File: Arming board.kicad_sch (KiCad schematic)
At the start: 22 parts, among them IC1 CD4043BDR, J3 Conn_01x04, Q1 SQS141ELNW-T1_GE3

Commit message: Basic routing and fixes
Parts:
- added H1, H2, H3, H4: MountingHole_Pad, MountingHole:MountingHole_3.2mm_M3_DIN965_Pad_TopBottom, symbol Mechanical:MountingHole_Pad
- C1, C2: value 1u -> 10u
- R3, R4: value 10k -> 1k
- R6, R7: value 10k -> 80k
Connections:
- net +BATT is gone; now on net VCC: D5.1 (K), D6.1 (K), J1.3 (Pin_3), J1.4 (Pin_4), J4.3 (Pin_3), J4.4 (Pin_4), Q1.1, Q1.2, Q1.3
- net GND: now also IC1.11 (R3), IC1.12 (S3), IC1.14 (S4), IC1.15 (R4), IC1.3 (R1), IC1.4 (S1), H1.1, H2.1, H3.1, H4.1
- net at D3.1 (K), R4.2: now also J3.3 (Pin_3); no longer J3.2 (Pin_2)
- net at D1.1 (K), R3.2: now also J3.2 (Pin_2); no longer J3.3 (Pin_3)

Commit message: improve routing
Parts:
- added TP1, TP2, TP3, TP4, TP5: TestPoint, TestPoint:TestPoint_Pad_D1.0mm, symbol Connector:TestPoint
- H1, H2, H3, H4, J1, J2, J3, J4, J5: now not fitted
- Q1: note (none) -> Out ot stock
- R1, R5: LCSC C25744 -> C100572
- R2: LCSC C11702 -> C100571
- R6, R7: LCSC C25744 -> (none)
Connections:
- net +BATT_ARM: now also TP5.1
- net VCC: now also TP4.1
- net arm: now also D1.1 (K), J3.2 (Pin_2), R3.2, TP2.1
- net disarm: now also D3.1 (K), J3.3 (Pin_3), R4.2, TP3.1
- net at IC1.9 (Q2), R2.1: now also TP1.1
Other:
- moved on the sheet: R1

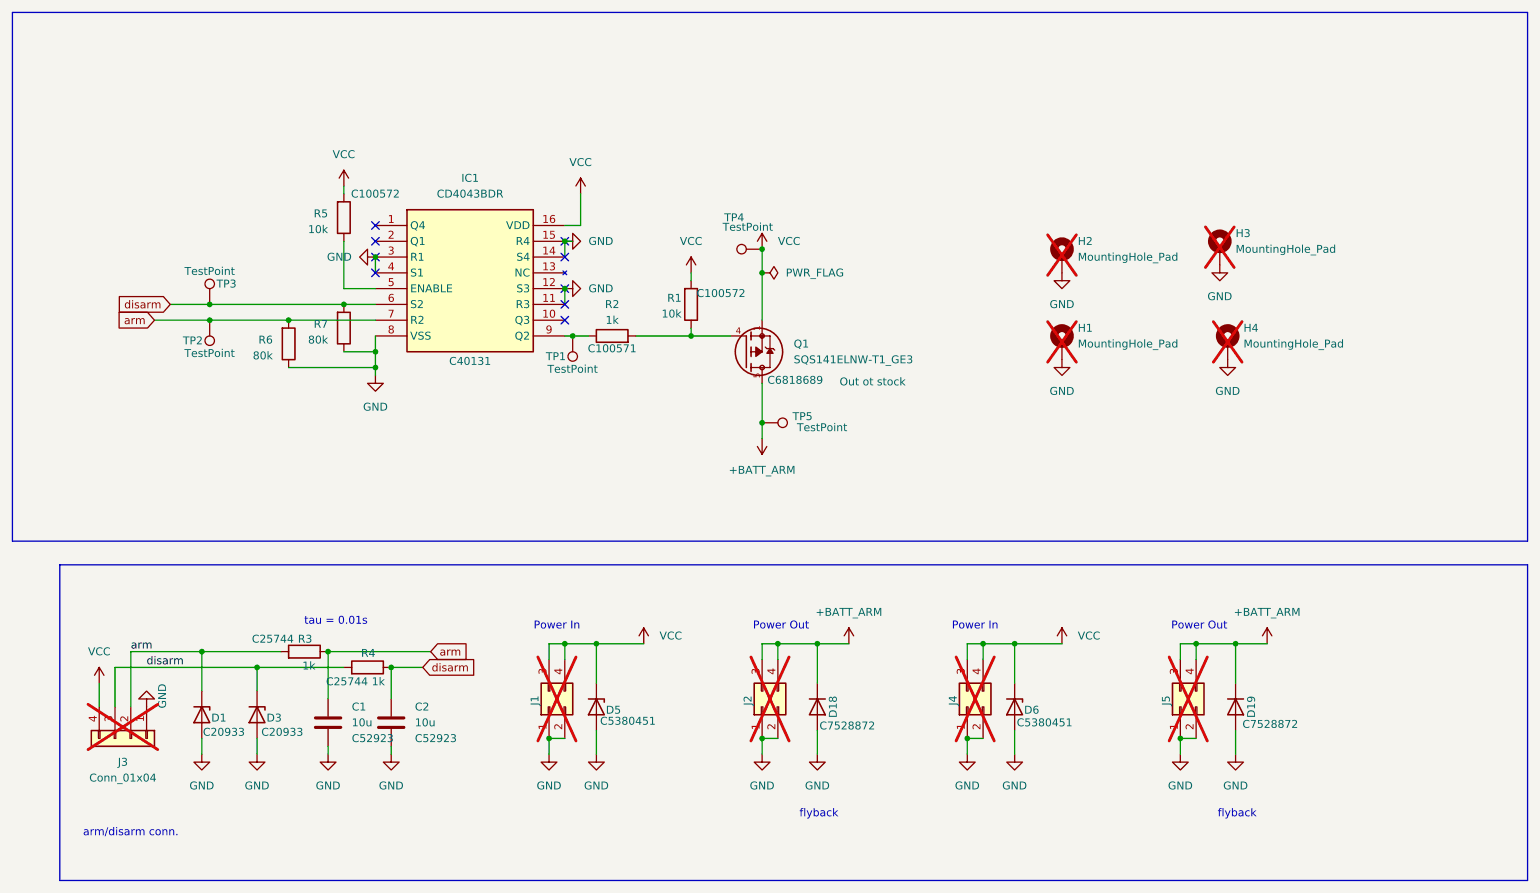
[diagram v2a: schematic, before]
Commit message: check parts, replace mosfet
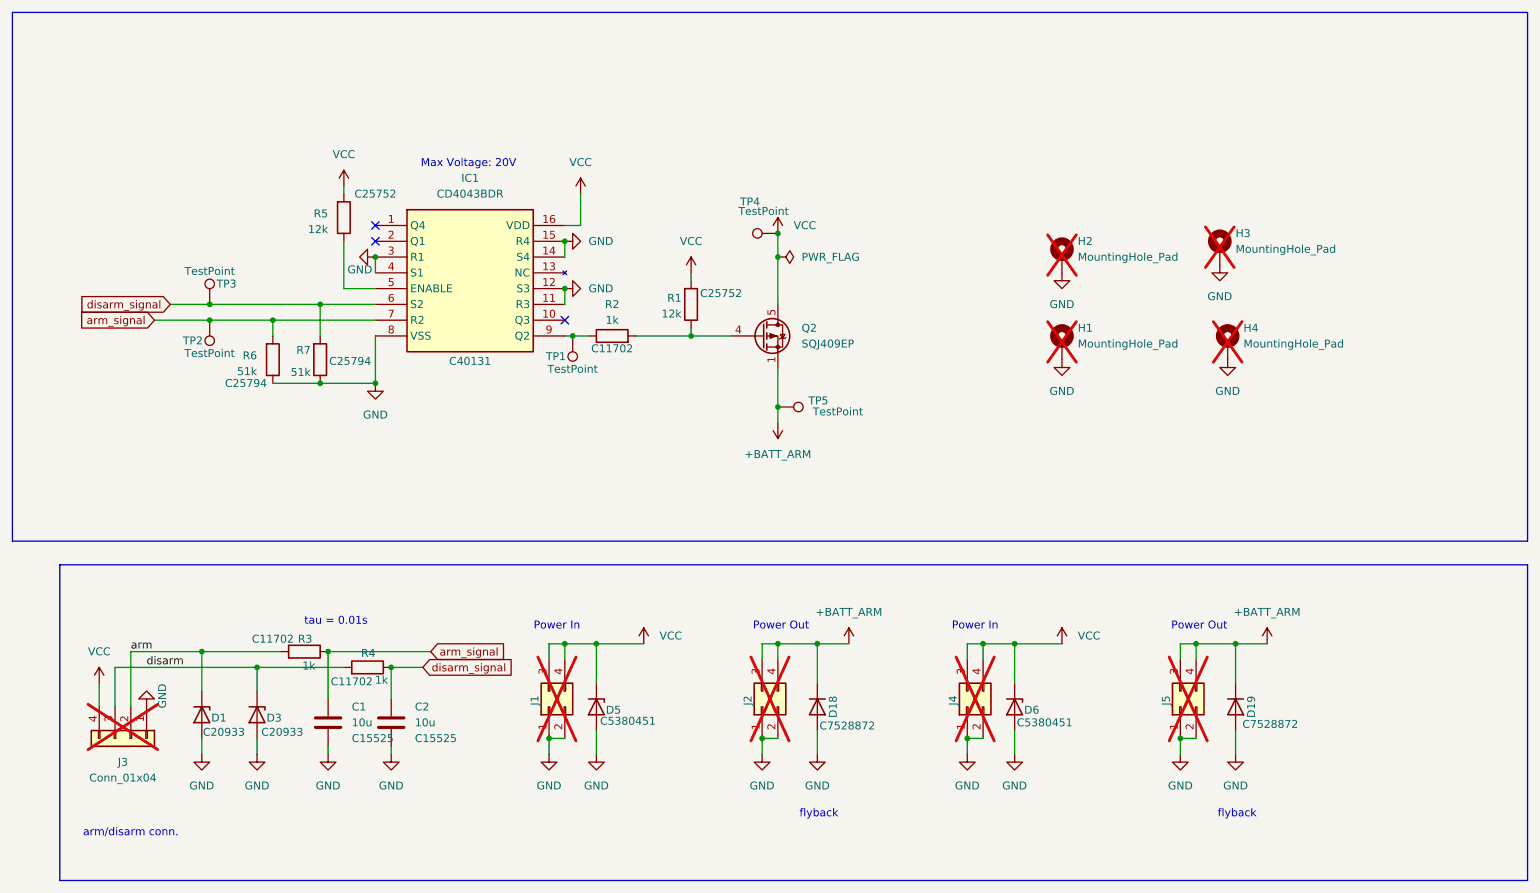
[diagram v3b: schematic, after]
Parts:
- removed Q1: SQS141ELNW-T1_GE3, Package_SO:PowerPAK_SO-8_Single, symbol SQS141ELNW-T1_GE3:SQS141ELNW-T1_GE3
- added Q2: SQJ409EP, Package_SO:PowerPAK_SO-8L_Single, symbol Transistor_FET:SQJ409EP
- C1, C2: LCSC C52923 -> C15525
- R1, R5: value 10k -> 12k; LCSC C100572 -> C25752
- R2: LCSC C100571 -> C11702
- R3, R4: LCSC C25744 -> C11702
- R6, R7: value 80k -> 51k; LCSC (none) -> C25794
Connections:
- net +BATT_ARM: now also Q2.1 (S), Q2.2 (S), Q2.3 (S)
- net VCC: now also Q2.5 (D)
- net arm: no longer C1.1, IC1.7 (R2), R3.1, R6.2, TP2.1
- net disarm: no longer C2.1, IC1.6 (S2), R4.1, R7.2, TP3.1
- net at R1.1, R2.2: now also Q2.4 (G)
- new net arm_signal: C1.1, IC1.7 (R2), R3.1, R6.2, TP2.1
- new net disarm_signal: C2.1, IC1.6 (S2), R4.1, R7.2, TP3.1
- no-connect marks 9 -> 3
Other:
- note added: "Max Voltage: 20V"
- moved on the sheet: R6, R7, TP4, TP5

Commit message: improve silkscreen
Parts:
- Q2: LCSC (none) -> C727776
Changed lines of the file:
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@@
+			)
+		)
+		(property "LCSC" "C727776"
+			(at 135.89 67.31 0)
+			(hide yes)
+			(show_name no)
+			(do_not_autoplace no)
+			(effects
+				(font
+					(size 1.27 1.27)
+				)
 			)
 		)

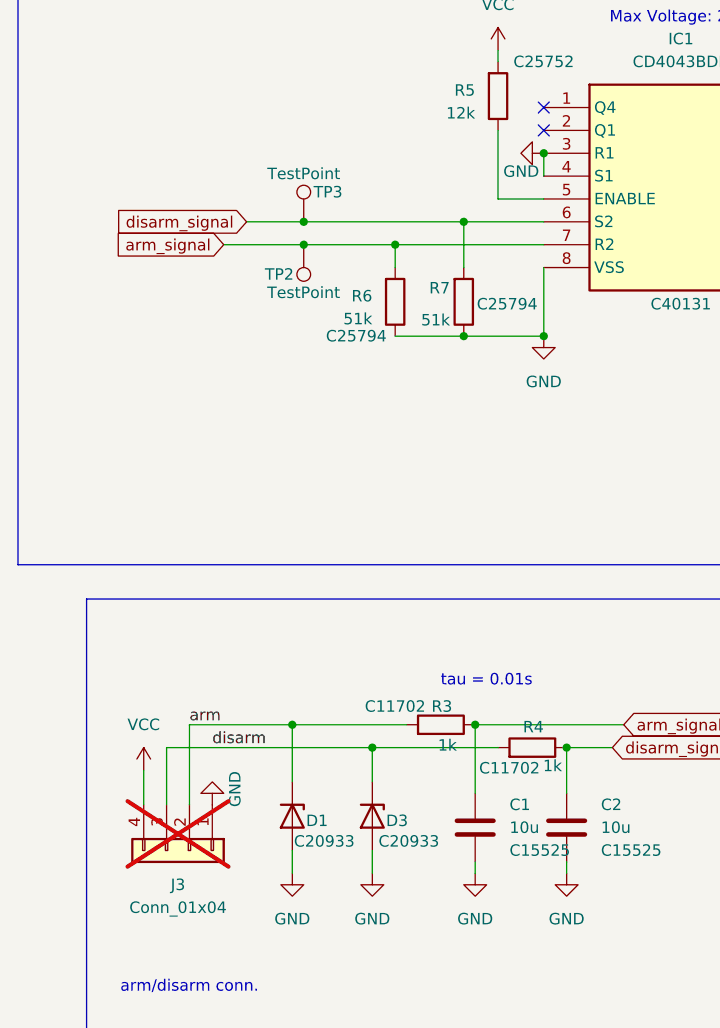
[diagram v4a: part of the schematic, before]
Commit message: change flipflop footprint
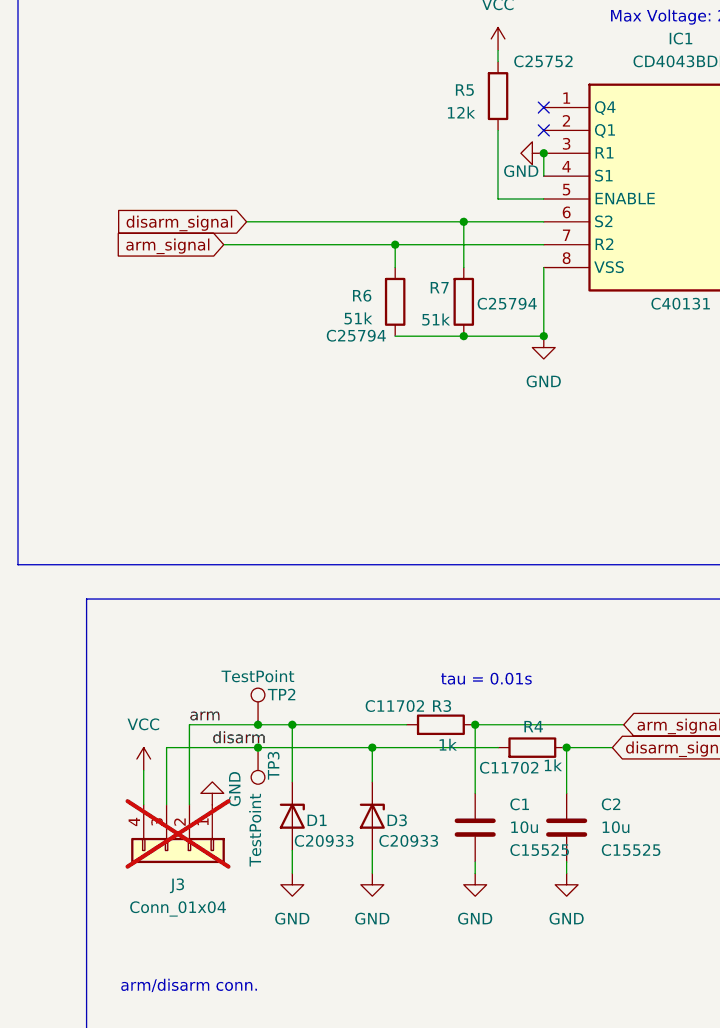
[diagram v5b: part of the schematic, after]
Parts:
- IC1: footprint Package_SO:SOIC-16W_7.5x10.3mm_P1.27mm -> Package_SO:SOIC-16_4.55x10.3mm_P1.27mm
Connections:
- net arm: now also TP2.1
- net arm_signal: no longer TP2.1
- net disarm: now also TP3.1
- net disarm_signal: no longer TP3.1
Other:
- moved on the sheet: TP2, TP3
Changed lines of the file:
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@@
 	)
 	(junction
+		(at 41.91 120.65)
+		(diameter 0)
+		(color 0 0 0 0)
+	)
+	(junction
 		(at 138.43 54.61)
 		(diameter 0)
@@
 	)
 	(junction
-		(at 205.74 116.84)
+		(at 45.72 118.11)
 		(diameter 0)
 		(color 0 0 0 0)
 	)
 	(junction
-		(at 144.78 116.84)
+		(at 205.74 116.84)
 		(diameter 0)
 		(color 0 0 0 0)
 	)
 	(junction
-		(at 45.72 118.11)
+		(at 144.78 116.84)
 		(diameter 0)
 		(color 0 0 0 0)
@@
 	)
 	(junction
-		(at 46.99 62.23)
-		(diameter 0)
-		(color 0 0 0 0)
-	)
-	(junction
 		(at 138.43 78.74)
 		(diameter 0)
@@
 	)
 	(junction
-		(at 46.99 64.77)
+		(at 41.91 118.11)
 		(diameter 0)
 		(color 0 0 0 0)
@@
 	(wire
 		(pts
-			(xy 31.75 120.65) (xy 54.61 120.65)
+			(xy 31.75 120.65) (xy 41.91 120.65)
 		)
 		(stroke
@@
 	(wire
 		(pts
-			(xy 46.99 62.23) (xy 64.77 62.23)
+			(xy 41.91 118.11) (xy 34.29 118.11)
 		)
 		(stroke
@@
 	(wire
 		(pts
-			(xy 45.72 118.11) (xy 34.29 118.11)
+			(xy 45.72 118.11) (xy 41.91 118.11)
 		)
 		(stroke
@@
 	(wire
 		(pts
-			(xy 40.64 62.23) (xy 46.99 62.23)
+			(xy 40.64 62.23) (xy 64.77 62.23)
 		)
 		(stroke
@@
 	(wire
 		(pts
-			(xy 38.1 64.77) (xy 46.99 64.77)
+			(xy 38.1 64.77) (xy 57.15 64.77)
 		)
 		(stroke
@@
 	(wire
 		(pts
+			(xy 41.91 120.65) (xy 54.61 120.65)
+		)
+		(stroke
+			(width 0)
+			(type default)
+		)
+	)
+	(wire
+		(pts
 			(xy 66.04 134.62) (xy 66.04 133.35)
 		)
@@
 	(wire
 		(pts
-			(xy 46.99 64.77) (xy 57.15 64.77)
-		)
-		(stroke
-			(width 0)
-			(type default)
-		)
-	)
-	(wire
-		(pts
 			(xy 203.2 132.08) (xy 205.74 132.08)
 		)
@@
 	(symbol
 		(lib_id "Connector:TestPoint")
-		(at 46.99 64.77 180)
+		(at 41.91 118.11 0)
 		(unit 1)
 		(body_style 1)
@@
 		(dnp no)
 		(property "Reference" "TP2"
-			(at 42.672 68.072 0)
+			(at 46.228 114.808 0)
 			(show_name no)
 			(do_not_autoplace no)
@@
 		)
 		(property "Value" "TestPoint"
-			(at 42.926 70.104 0)
+			(at 45.974 112.776 0)
 			(show_name no)
 			(do_not_autoplace no)
@@
 		)
 		(property "Footprint" "TestPoint:TestPoint_Pad_D1.0mm"
-			(at 41.91 64.77 0)
+			(at 46.99 118.11 0)
 			(hide yes)
 			(show_name no)
@@
 		)
 		(property "Datasheet" ""
-			(at 41.91 64.77 0)
+			(at 46.99 118.11 0)
 			(hide yes)
 			(show_name no)
@@
 		)
 		(property "Description" "test point"
-			(at 46.99 64.77 0)
+			(at 41.91 118.11 0)
 			(hide yes)
 			(show_name no)
@@
 			)
 		)
-		(property "Footprint" "Package_SO:SOIC-16W_7.5x10.3mm_P1.27mm"
+		(property "Footprint" "Package_SO:SOIC-16_4.55x10.3mm_P1.27mm"
 			(at 100.33 144.45 0)
 			(hide yes)
@@
 	(symbol
 		(lib_id "Connector:TestPoint")
-		(at 46.99 62.23 0)
+		(at 41.91 120.65 180)
 		(unit 1)
 		(body_style 1)
@@
 		(dnp no)
 		(property "Reference" "TP3"
-			(at 51.308 58.928 0)
+			(at 43.688 124.206 90)
 			(show_name no)
 			(do_not_autoplace no)
@@
 		)
 		(property "Value" "TestPoint"
-			(at 51.054 56.896 0)
+			(at 41.656 133.858 90)
 			(show_name no)
 			(do_not_autoplace no)
@@
 		)
 		(property "Footprint" "TestPoint:TestPoint_Pad_D1.0mm"
-			(at 52.07 62.23 0)
+			(at 36.83 120.65 0)
 			(hide yes)
 			(show_name no)
@@
 		)
 		(property "Datasheet" ""
-			(at 52.07 62.23 0)
+			(at 36.83 120.65 0)
 			(hide yes)
 			(show_name no)
@@
 		)
 		(property "Description" "test point"
-			(at 46.99 62.23 0)
+			(at 41.91 120.65 0)
 			(hide yes)
 			(show_name no)
